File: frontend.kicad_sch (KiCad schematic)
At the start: 70 parts, among them J10 GND_CLIP, J2 RF-SHIELD-COVER, J3 RF-SHIELD-FRAME, J4 MOUNTING_HOLE, J5 MOUNTING_HOLE, J6 MOUNTING_HOLE, J7 MOUNTING_HOLE, P4 SMA, Q1 NMOS/PMOS, U1 MXD8546F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

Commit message: Use lumped element filters for image rejection
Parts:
- removed U3: LOWPASS_FILTER, hackrf:GSG-LP0603, symbol hackrf:FIL-LP0603
- removed U8: HIGHPASS_FILTER, hackrf:GSG-HP-DEA, symbol hackrf:FIL-DEA
- added C101, C103, C51, C61: 0.7±0.05 pF, Capacitor_SMD:C_0201_0603Metric, symbol Device:C
- added C54, C56: 1.8±0.05 pF, Capacitor_SMD:C_0201_0603Metric, symbol Device:C
- added C91, C96: 1.6±0.05 pF, Capacitor_SMD:C_0201_0603Metric, symbol Device:C
- added L14: 5.6±3% nH, Inductor_SMD:L_0201_0603Metric, symbol Device:L
- added L15, L8: 4.7±3% nH, Inductor_SMD:L_0201_0603Metric, symbol Device:L
- added L16, L17: 1.8±0.05 nH, Inductor_SMD:L_0201_0603Metric, symbol Device:L
- added L18: 1.6±0.05 nH, Inductor_SMD:L_0201_0603Metric, symbol Device:L
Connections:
- net GND: now also C51.2, C54.2, C56.2, C61.2, L16.2, L17.2, L18.2
- net at U1.9 (RF4): now also C91.1
- net at U9.3 (RF1): now also C96.2
- net at U9.2 (RF3): now also C61.1, L15.1
- net at U1.11 (RF3): now also C51.1, L8.2
- new net: C101.1, C91.2, L16.1
- new net: C54.1, L14.2, L8.1
- new net: C103.2, C96.1, L17.1
- new net: C56.1, L14.1, L15.2
- new net: C101.2, C103.1, L18.1
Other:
- moved on the sheet: C11, C16, C18, C19, C20, C29, C9, U1, U2, U5, U6, U7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

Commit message: Add IF filters
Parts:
- added FL2, FL3: BPF, praline:Filter_Pulse_BPF1608LM09R5000A, symbol RF_Filter:BFCN-1445
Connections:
- net GND: now also FL2.2 (GND), FL2.4 (GND), FL3.2 (GND), FL3.4 (GND)
- net IF: now also FL3.1 (IN); no longer U7.5 (RFIN)
- net MIX_BYPASS: now also FL2.3 (OUT); no longer U2.11 (RF3)
- new net: FL3.3 (OUT), U7.5 (RFIN)
- new net: FL2.1 (IN), U2.11 (RF3)
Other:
- moved on the sheet: C101, C103, C11, C16, C18, C19, C20, C29, C51, C54, C56, C61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

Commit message: Connect mixer U4 LD and ENBL pins to MCU
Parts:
- removed C10, C17, C21, C7, C8: 1uF, Capacitor_SMD:C_0201_0603Metric, symbol Device:C
- removed C101, C103, C51, C61: 0.7±0.05 pF, Capacitor_SMD:C_0201_0603Metric, symbol Device:C
- removed C11, C16, C18, C19, C20, C29, C9: 3.3nF, Capacitor_SMD:C_0201_0603Metric, symbol Device:C
- removed C31: 1 uF, Capacitor_SMD:C_0201_0603Metric, symbol Device:C
- removed C54, C56: 1.8±0.05 pF, Capacitor_SMD:C_0201_0603Metric, symbol Device:C
- removed C91, C96: 1.6±0.05 pF, Capacitor_SMD:C_0201_0603Metric, symbol Device:C
- removed FL2, FL3: BPF, praline:Filter_Pulse_BPF1608LM09R5000A, symbol RF_Filter:BFCN-1445
- removed L14: 5.6±3% nH, Inductor_SMD:L_0201_0603Metric, symbol Device:L
- removed L15, L8: 4.7±3% nH, Inductor_SMD:L_0201_0603Metric, symbol Device:L
- removed L16, L17: 1.8±0.05 nH, Inductor_SMD:L_0201_0603Metric, symbol Device:L
- removed L18: 1.6±0.05 nH, Inductor_SMD:L_0201_0603Metric, symbol Device:L
- removed U1, U2: MXD8546F, praline:QFN-12-1EP_2x2mm_P0.5mm_EP1x1mm, symbol praline:MXD8546F
- removed U5, U6, U7: FM8625H, praline:TSLP-6-4_1.1x0.7mm_P0.4mm, symbol praline:BGS12P2L6
- removed U9: MXD8638C, praline:TSNP-9-3, symbol praline:MXD8638
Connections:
- net RF: now reaches U12.4 (ANT)
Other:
- removed sheet Mixer
- note removed: "image reject filters"
- moved on the sheet: C160, C161, C171, C2, C4, C50, C52, C53, C55, C57, C58, C59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

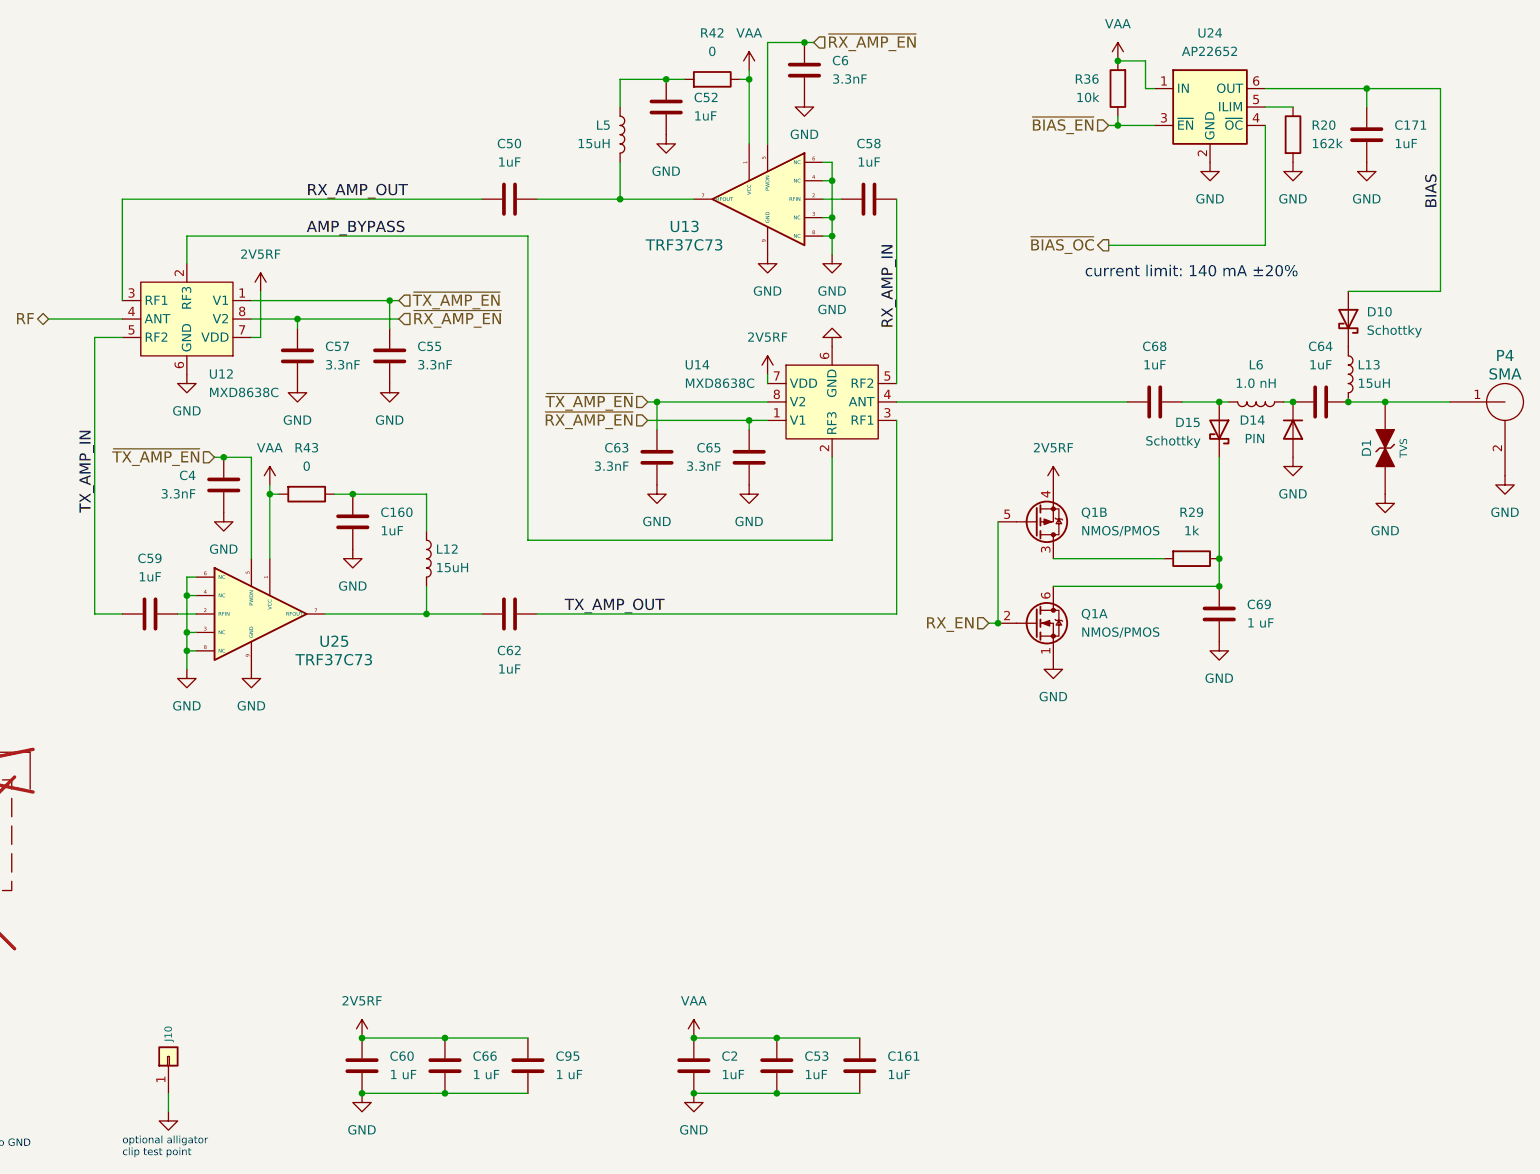
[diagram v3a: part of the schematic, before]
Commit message: Improve power supply filtering and decoupling
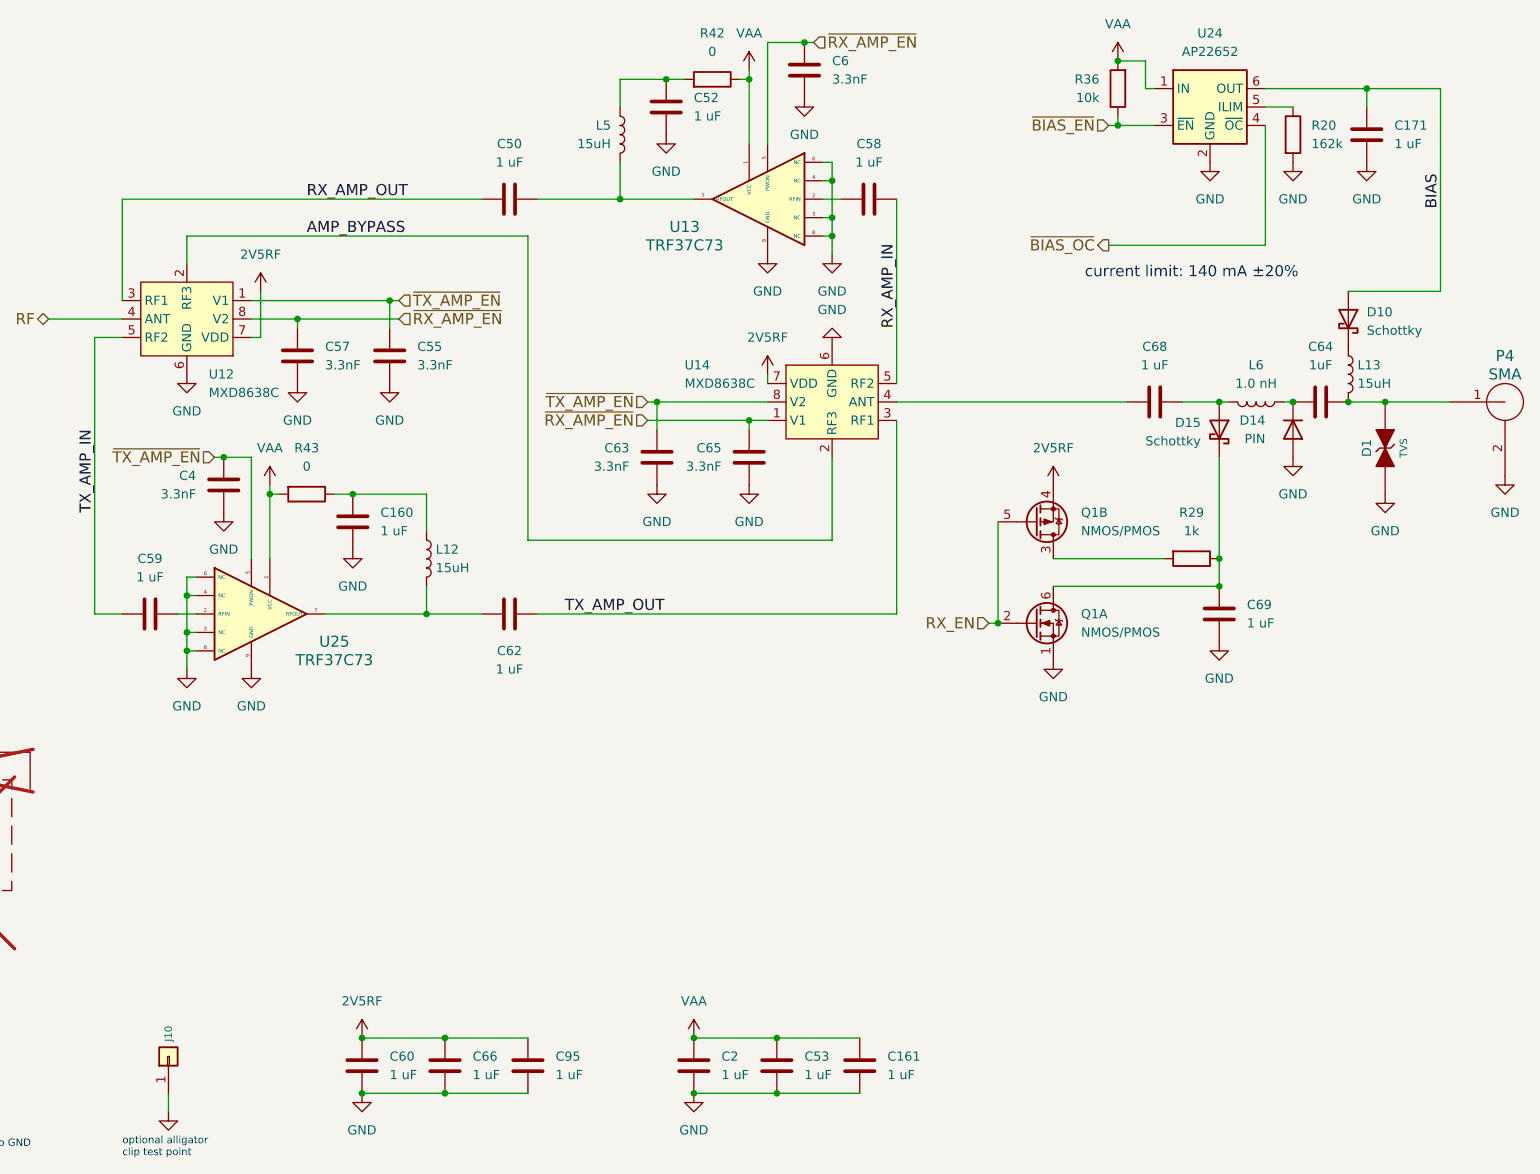
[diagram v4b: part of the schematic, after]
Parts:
- C160, C161, C171, C2, C50, C52, C53, C58, C59, C62, C68: value 1uF -> 1 uF
- C60, C66, C69, C95: Substitution (none) -> GRM033R61A105ME44*, GRM033R61C105ME15*, Samsung CL03A105MO3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
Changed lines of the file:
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@@
 			)
 		)
-		(property "Value" "1uF"
+		(property "Value" "1 uF"
 			(at 137.16 50.7999 0)
 			(effects
@@
 			)
 		)
-		(property "Value" "1uF"
+		(property "Value" "1 uF"
 			(at 163.83 182.8799 0)
 			(effects
@@
 			)
 		)
-		(property "Value" "1uF"
+		(property "Value" "1 uF"
 			(at 93.98 107.9499 0)
 			(effects
@@
 			)
 		)
-		(property "Value" "1uF"
+		(property "Value" "1 uF"
 			(at 152.4 182.8799 0)
 			(effects
@@
 			)
 		)
-		(property "Value" "1uF"
+		(property "Value" "1 uF"
 			(at 161.29 57.15 90)
 			(effects
@@
 			)
 		)
-		(property "Value" "1uF"
+		(property "Value" "1 uF"
 			(at 111.76 57.15 90)
 			(effects
@@
 			)
 		)
-		(property "Value" "1uF"
+		(property "Value" "1 uF"
 			(at 62.23 114.3 90)
 			(effects
@@
 			)
 		)
-		(property "Value" "1uF"
+		(property "Value" "1 uF"
 			(at 111.76 127 90)
 			(effects
@@
 			)
 		)
-		(property "Value" "1uF"
+		(property "Value" "1 uF"
 			(at 233.68 54.6099 0)
 			(effects
@@
 			)
 		)
-		(property "Value" "1uF"
+		(property "Value" "1 uF"
 			(at 140.97 182.8799 0)
 			(effects
@@
 			)
 		)
-		(property "Description" ""
+		(property "Description" "CAP CER 1UF 10V X5R 0201"
 			(at 102.87 181.61 0)
 			(effects
@@
 			)
 		)
+		(property "Substitution" "GRM033R61A105ME44*, GRM033R61C105ME15*, Samsung CL03A105MO3NRN*"
+			(at 102.87 181.61 0)
+			(effects
+				(font
+					(size 1.27 1.27)
+				)
+				(hide yes)
+			)
+		)
 		(pin "1"
 		)
@@
 			)
 		)
-		(property "Description" ""
+		(property "Description" "CAP CER 1UF 10V X5R 0201"
 			(at 209.55 119.38 0)
 			(effects
@@
 			)
 		)
+		(property "Substitution" "GRM033R61A105ME44*, GRM033R61C105ME15*, Samsung CL03A105MO3NRN*"
+			(at 209.55 119.38 0)
+			(effects
+				(font
+					(size 1.27 1.27)
+				)
+				(hide yes)
+			)
+		)
 		(pin "1"
 		)
@@
 			)
 		)
-		(property "Value" "1uF"
+		(property "Value" "1 uF"
 			(at 200.66 85.09 90)
 			(effects
@@
 			)
 		)
-		(property "Description" ""
+		(property "Description" "CAP CER 1UF 10V X5R 0201"
 			(at 114.3 181.61 0)
 			(effects
@@
 			)
 		)
+		(property "Substitution" "GRM033R61A105ME44*, GRM033R61C105ME15*, Samsung CL03A105MO3NRN*"
+			(at 114.3 181.61 0)
+			(effects
+				(font
+					(size 1.27 1.27)
+				)
+				(hide yes)
+			)
+		)
 		(pin "1"
 		)
@@
 			)
 		)
-		(property "Description" ""
+		(property "Description" "CAP CER 1UF 10V X5R 0201"
 			(at 91.44 181.61 0)
 			(effects
@@
 			(at 91.44 181.61 0)
 			(effects
+				(font
+					(size 1.27 1.27)
+				)
+				(hide yes)
+			)
+		)
+		(property "Substitution" "GRM033R61A105ME44*, GRM033R61C105ME15*, Samsung CL03A105MO3NRN*"
+			(at 91.44 181.61 0)
+			(effects

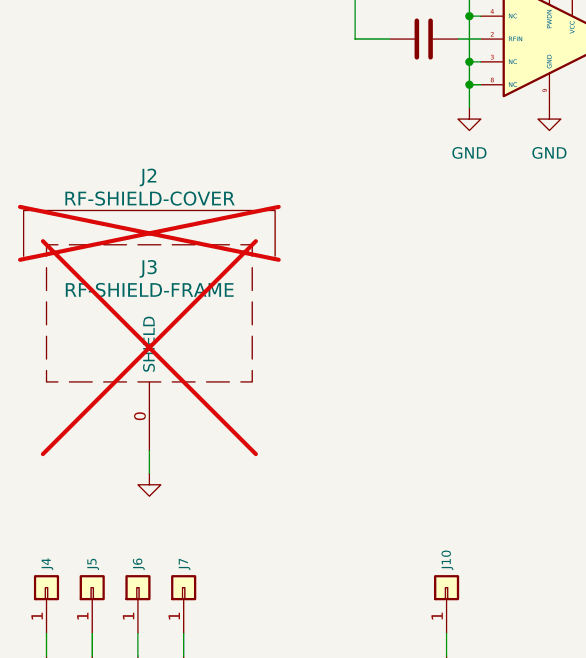
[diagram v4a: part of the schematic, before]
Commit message: Adjust shield footprint for improved routing
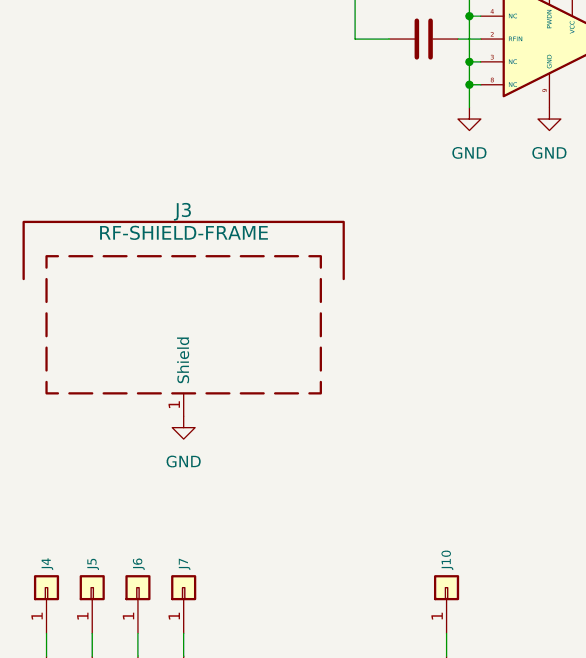
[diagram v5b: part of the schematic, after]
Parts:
- removed J2: RF-SHIELD-COVER, symbol hackrf:RF-SHIELD-COVER
- J3: footprint hackrf:GSG-SHIELD-BMI-S-230 -> praline:Laird_Technologies_BMI-S-230-F_50.8x38.1mm; symbol hackrf:RF-SHIELD-FRAME -> Device:RFShield_TwoPieces; now fitted
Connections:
- net GND: now also J3.1 (Shield); no longer J3.0 (SHIELD)
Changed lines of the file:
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@@
 	(wire
 		(pts
-			(xy 31.75 165.1) (xy 31.75 167.64)
-		)
-		(stroke
-			(width 0)
-			(type default)
-		)
-	)
-	(wire
-		(pts
 			(xy 67.31 124.46) (xy 68.58 124.46)
 		)
@@
 	)
 	(symbol
-		(lib_id "hackrf:RF-SHIELD-COVER")
-		(at 31.75 140.97 0)
-		(unit 1)
-		(exclude_from_sim no)
-		(in_bom yes)
-		(on_board no)
-		(dnp yes)
-		(property "Reference" "J2"
-			(at 31.75 134.62 0)
-			(effects
-				(font
-					(size 1.524 1.524)
-				)
-			)
-		)
-		(property "Value" "RF-SHIELD-COVER"
-			(at 31.75 137.16 0)
-			(effects
-				(font
-					(size 1.524 1.524)
-				)
-			)
-		)
-		(property "Footprint" ""
-			(at 31.75 140.97 0)
-			(effects
-				(font
-					(size 1.524 1.524)
-				)
-				(hide yes)
-			)
-		)
-		(property "Datasheet" "~"
-			(at 31.75 140.97 0)
-			(effects
-				(font
-					(size 1.524 1.524)
-				)
-			)
-		)
-		(property "Description" "BOARD SHIELD 2INX1.5IN COVER"
-			(at 31.75 140.97 0)
-			(effects
-				(font
-					(size 1.524 1.524)
-				)
-				(hide yes)
-			)
-		)
-		(property "Manufacturer" "Laird"
-			(at 31.75 140.97 0)
-			(effects
-				(font
-					(size 1.524 1.524)
-				)
-				(hide yes)
-			)
-		)
-		(property "Part Number" "BMI-S-230-C"
-			(at 31.75 140.97 0)
-			(effects
-				(font
-					(size 1.524 1.524)
-				)
-				(hide yes)
-			)
-		)
-		(instances
-			(project "praline"
-				(path "/dba4afc6-760f-46cb-a936-032b76448f03/00000000-0000-0000-0000-0000503bb638"
-					(reference "J2")
-					(unit 1)
-				)
-			)
-		)
-	)
-	(symbol
 		(lib_id "praline:Q_Dual_NMOS_PMOS_S1G1D2S2G2D1")
 		(at 184.15 106.68 0)
@@
 	)
 	(symbol
+		(lib_id "power:GND")
+		(at 35.56 161.29 0)
+		(unit 1)
+		(exclude_from_sim no)
+		(in_bom yes)
+		(on_board yes)
+		(dnp no)
+		(fields_autoplaced yes)
+		(property "Reference" "#PWR058"
+			(at 35.56 167.64 0)
+			(effects
+				(font
+					(size 1.27 1.27)
+				)
+				(hide yes)
+			)
+		)
+		(property "Value" "GND"
+			(at 35.56 166.37 0)
+			(effects
+				(font
+					(size 1.27 1.27)
+				)
+			)
+		)
+		(property "Footprint" ""
+			(at 35.56 161.29 0)
+			(effects
+				(font
+					(size 1.27 1.27)
+				)
+				(hide yes)
+			)
+		)
+		(property "Datasheet" ""
+			(at 35.56 161.29 0)
+			(effects
+				(font
+					(size 1.27 1.27)
+				)
+				(hide yes)
+			)
+		)
+		(property "Description" "Power symbol creates a global label with name \"GND\" , ground"
+			(at 35.56 161.29 0)
+			(effects
+				(font
+					(size 1.27 1.27)
+				)
+				(hide yes)
+			)
+		)
+		(pin "1"
+		)
+		(instances
+			(project "praline"
+				(path "/dba4afc6-760f-46cb-a936-032b76448f03/00000000-0000-0000-0000-0000503bb638"
+					(reference "#PWR058")
+					(unit 1)
+				)
+			)
+		)
+	)
+	(symbol
 		(lib_id "Device:R")
 		(at 139.7 45.72 270)
@@
 	)
 	(symbol
-		(lib_id "power:GND")
-		(at 31.75 167.64 0)
-		(unit 1)
-		(exclude_from_sim no)
-		(in_bom yes)
-		(on_board yes)
-		(dnp no)
-		(property "Reference" "#PWR058"
-			(at 31.75 167.64 0)
-			(effects
-				(font
-					(size 0.762 0.762)
-				)
-				(hide yes)
-			)
-		)
-		(property "Value" "GND"
-			(at 31.75 169.418 0)
-			(effects
-				(font
-					(size 0.762 0.762)
-				)
-				(hide yes)
-			)
-		)
-		(property "Footprint" ""
-			(at 31.75 167.64 0)
-			(effects
-				(font
-					(size 1.524 1.524)
-				)
-			)
-		)
-		(property "Datasheet" ""
-			(at 31.75 167.64 0)
-			(effects
-				(font
-					(size 1.524 1.524)
-				)
-			)
-		)
-		(property "Description" "Power symbol creates a global label with name \"GND\" , ground"
-			(at 31.75 167.64 0)
-			(effects
-				(font
-					(size 1.27 1.27)
-				)
-				(hide yes)
-			)
-		)
-		(pin "1"
-		)
-		(instances
-			(project "praline"
-				(path "/dba4afc6-760f-46cb-a936-032b76448f03/00000000-0000-0000-0000-0000503bb638"
-					(reference "#PWR058")
-					(unit 1)
-				)
-			)
-		)
-	)
-	(symbol
 		(lib_id "Device:C")
 		(at 91.44 181.61 0)
@@
 	)
 	(symbol
-		(lib_id "hackrf:RF-SHIELD-FRAME")
-		(at 31.75 157.48 0)
+		(lib_id "Device:RFShield_TwoPieces")
+		(at 35.56 151.13 0)
 		(unit 1)
 		(exclude_from_sim no)
 		(in_bom yes)
 		(on_board yes)
-		(dnp yes)
+		(dnp no)
 		(property "Reference" "J3"
-			(at 31.75 144.78 0)
+			(at 35.56 138.43 0)
 			(effects
 				(font
@@
 		)
 		(property "Value" "RF-SHIELD-FRAME"
-			(at 31.75 147.32 0)
+			(at 35.56 140.97 0)
 			(effects
 				(font
@@
 			)
 		)
-		(property "Footprint" "hackrf:GSG-SHIELD-BMI-S-230"
-			(at 31.75 157.48 0)
+		(property "Footprint" "praline:Laird_Technologies_BMI-S-230-F_50.8x38.1mm"
+			(at 35.56 151.13 0)
 			(effects
 				(font
@@
 		)
 		(property "Datasheet" "~"
-			(at 31.75 157.48 0)
+			(at 35.56 151.13 0)
 			(effects
 				(font
@@
 		)
 		(property "Description" "BOARD SHIELD 2INX1.5IN FRAME"
-			(at 31.75 157.48 0)
+			(at 35.56 151.13 0)
 			(effects
 				(font
@@
 		)
 		(property "Manufacturer" "Laird"
-			(at 31.75 157.48 0)
+			(at 35.56 151.13 0)
 			(effects
 				(font
@@
 		)
 		(property "Part Number" "BMI-S-230-F-R"
-			(at 31.75 157.48 0)
+			(at 35.56 151.13 0)
 			(effects
 				(font
@@
 			)
 		)
-		(pin "0"
+		(pin "1"
 		)
 		(instances
